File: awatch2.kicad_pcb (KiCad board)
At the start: 4 copper layers, 73.4 x 64.4 mm, 169 parts, among them J101 Conn_01x02, J102 Conn_01x02, J103 Conn_01x02, J104 Conn_01x02, J301 Conn_01x02, J801 Molex 1050170001, J802 Conn_01x06, Q701 FDV301N, SW101 B3S-1000, SW102 B3S-1000, SW103 B3S-1000, SW104 B3S-1000, U1 nRF52840, U301 MAX14690, U401 W25Q128JVPIQTR, U501 BMM150, U502 APDS-9306-065, U503 BMI160, U504 BMP388, U601 SPK0641HT4H-1, U701 AYF531035 (LS013B7DH05), U801 AT93C46DN-SH-T, U802 MCP1703A-3302_SOT223, U803 FT2232HL, U901 DRV2604, X1 ABM11W-32.0000MHZ-8-B1U-T3, Y801 FH1200004

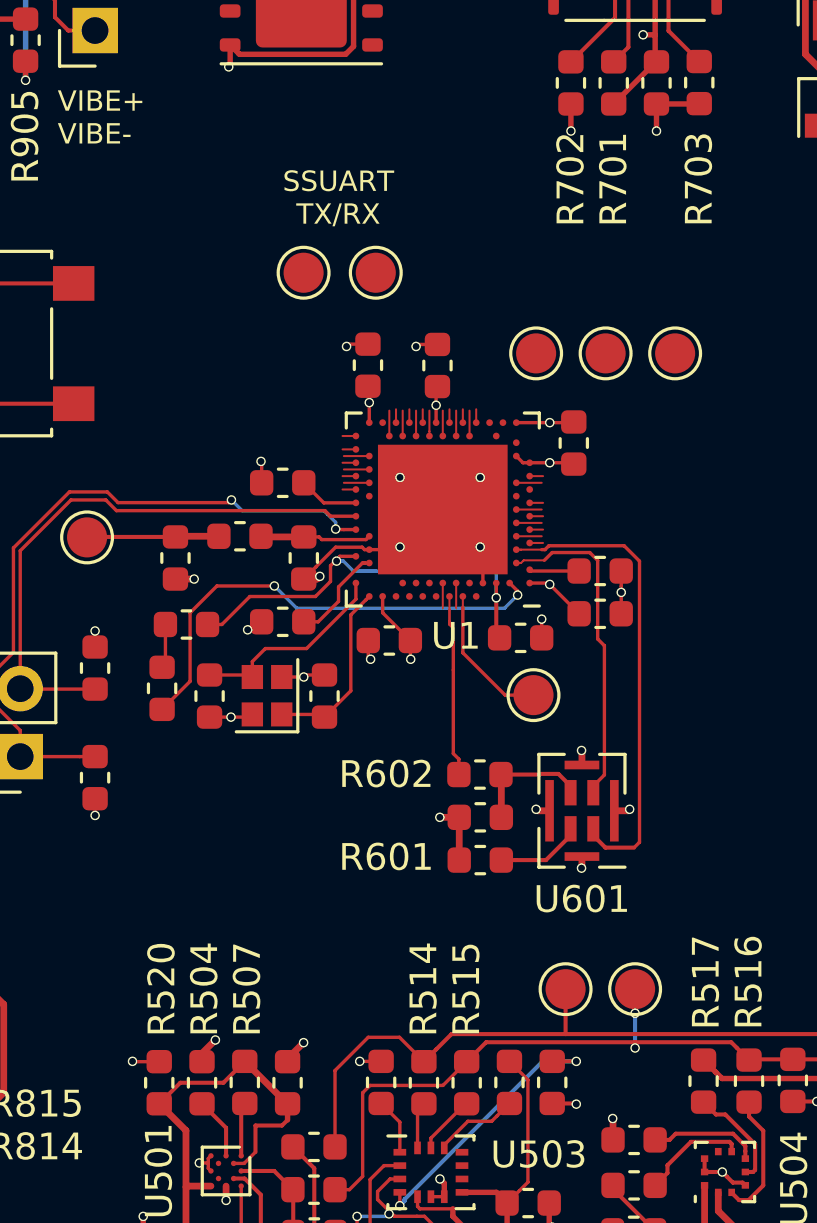
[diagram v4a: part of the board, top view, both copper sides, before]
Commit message: nRF pinout changes for routability
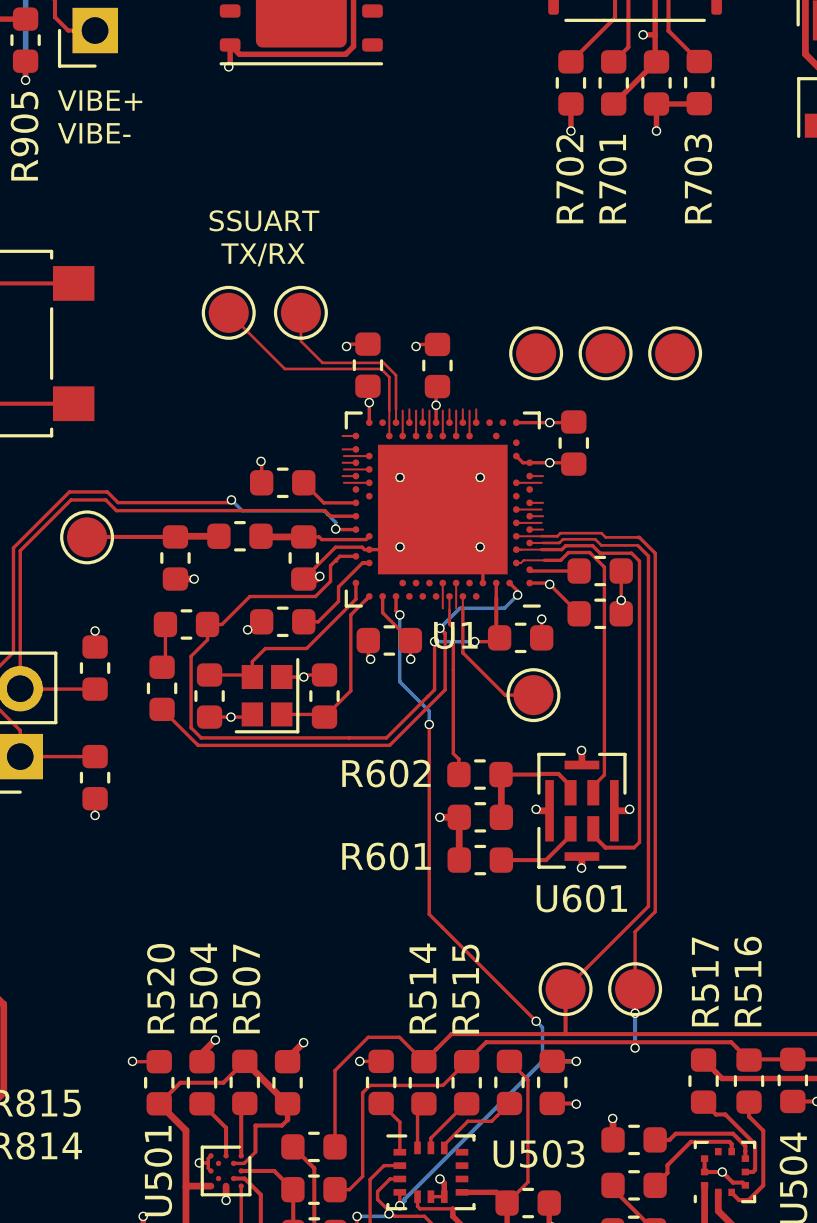
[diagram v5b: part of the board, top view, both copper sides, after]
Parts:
- moved TP108 3.18 mm to (81.5, 51.5)
- moved TP109 3.18 mm to (84.2, 51.5)
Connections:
- U1 pad A20: Net-(U1-PadA20) -> /Sensors/SENS_IMU_INT
- U1 pad G1: /FTDI USB Debug/UARTDBG_RX -> /Sensors/SENS_SDA
- U1 pad H2: /FTDI USB Debug/UARTDBG_TX -> /Sensors/SENS_SCL
- U1 pad L1: /Sensors/SENS_SCL -> /FTDI USB Debug/UARTDBG_RX
- U1 pad N1: /Sensors/SENS_SDA -> /FTDI USB Debug/UARTDBG_TX
- U1 pad R24: /Sensors/SENS_IMU_INT -> Net-(U1-PadR24)
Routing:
- net /Sensors/SENS_SDA: track 39.7 -> 61.5 mm
- net /Sensors/SENS_SCL: track 26.8 -> 48.5 mm
- net /Sensors/SENS_IMU_INT: track 10.8 -> 29.9 mm, vias 2 -> 5
- net Net-(C15-Pad2): track 16.2 -> 27.5 mm
- net /nRF52840/UARTSS_TX: track 0.95 -> 9.20 mm
- net /nRF52840/UARTSS_RX: track 0.50 -> 6.92 mm
- net Net-(L2-Pad2): track 17.8 -> 18.4 mm

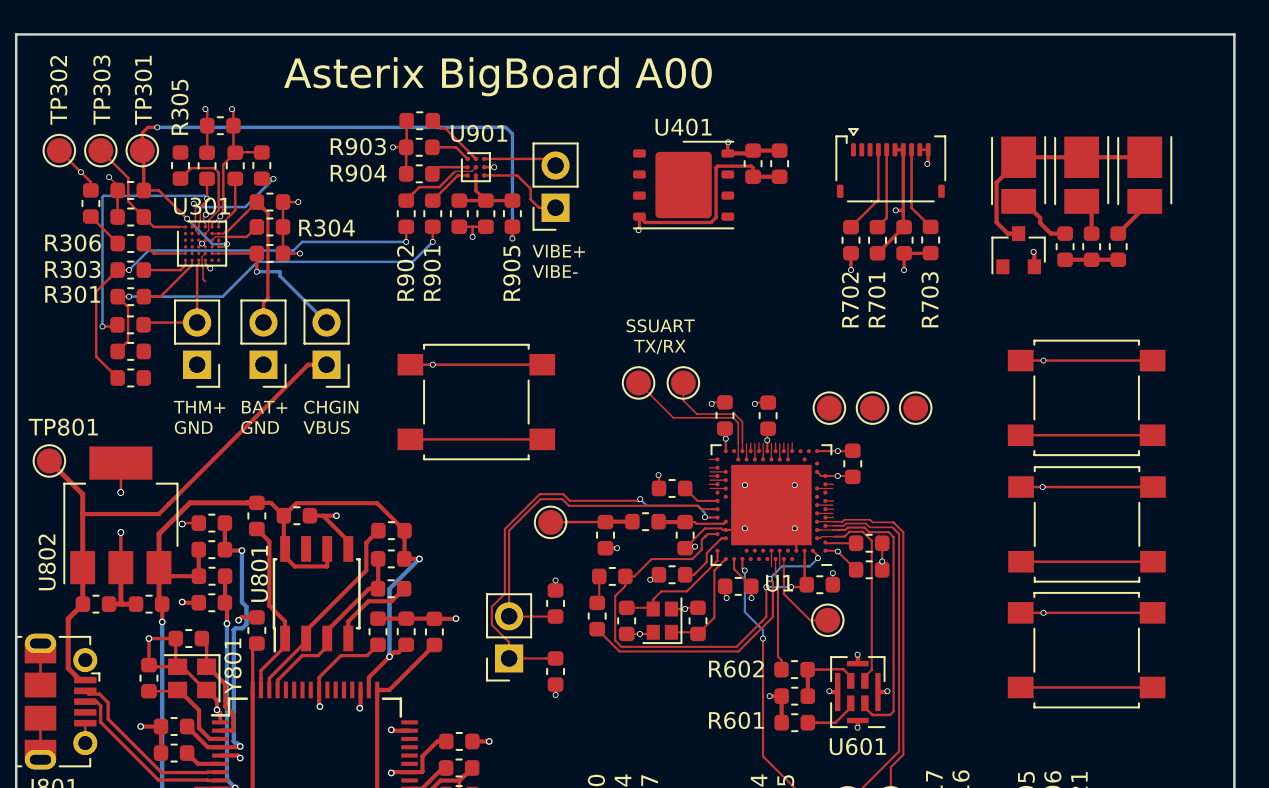
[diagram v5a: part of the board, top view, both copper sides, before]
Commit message: some PMIC and sensor routing
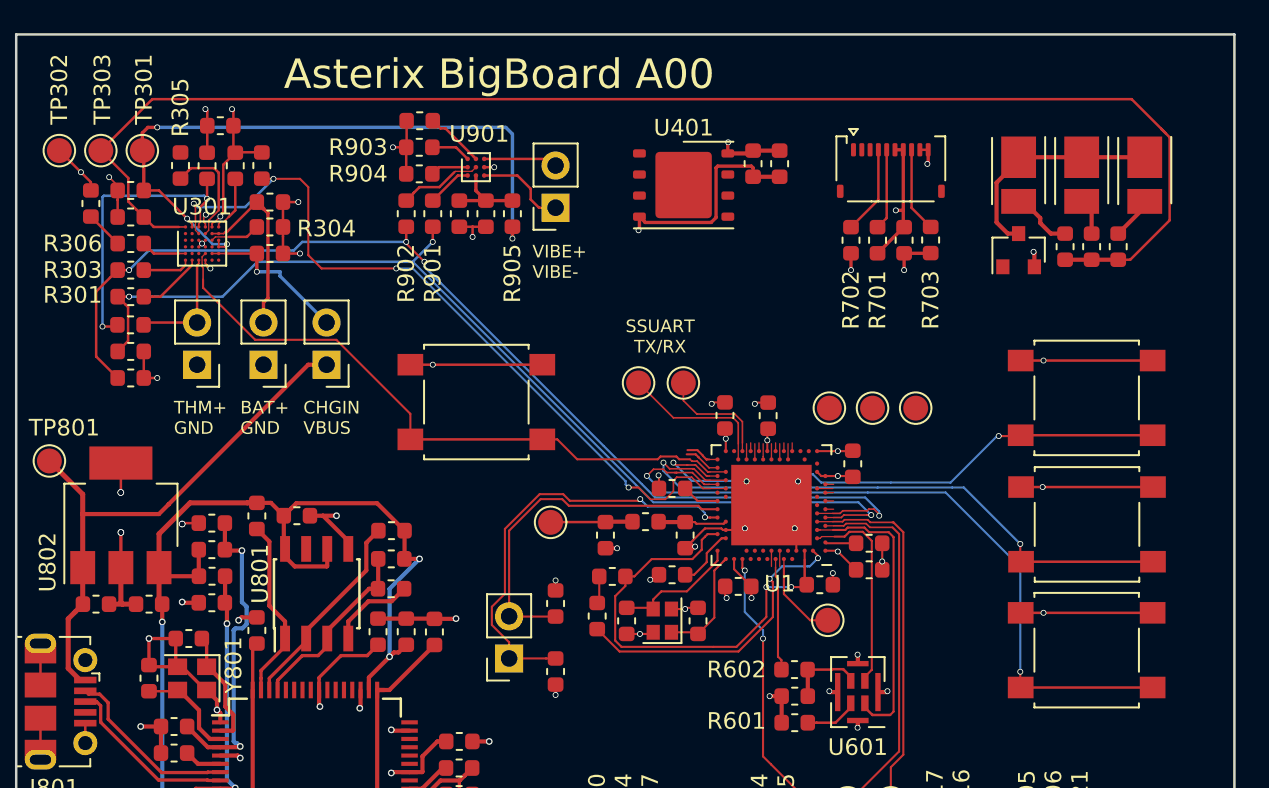
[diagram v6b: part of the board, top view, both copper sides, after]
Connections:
- U1 pad M2: /nRF52840/NRF_CHICKEN0 -> Net-(U1-PadM2)
- U1 pad R1: Net-(U1-PadR1) -> /nRF52840/NRF_CHICKEN0
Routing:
- net +3.3V: track 11.0 -> 87.1 mm
- net /PMIC/PMIC_SDA: track 27.5 -> 67.1 mm, vias 2 -> 4
- net /PMIC/PMIC_INTn: track 9.33 -> 47.4 mm, vias 2 -> 4
- net /nRF52840/BTN_DOWN: track 8.45 -> 44.9 mm, vias 0 -> 2
- net /PMIC/PMIC_SCL: track 25.6 -> 61.9 mm, vias 2 -> 3
- net /PMIC/BTN_BACK: track 10.8 -> 39.3 mm
- net /nRF52840/BTN_CENTER: track 8.90 -> 37.1 mm, vias 0 -> 2
- net /nRF52840/BTN_UP: track 8.45 -> 33.9 mm, vias 0 -> 2
- net +2V8: track 61.6 -> 64.0 mm, vias 22 -> 23
- net /FTDI USB Debug/NRF_SWDCLK: track 28.3 -> 30.0 mm
- net /FTDI USB Debug/NRF_SWDIO: track 35.0 -> 36.6 mm

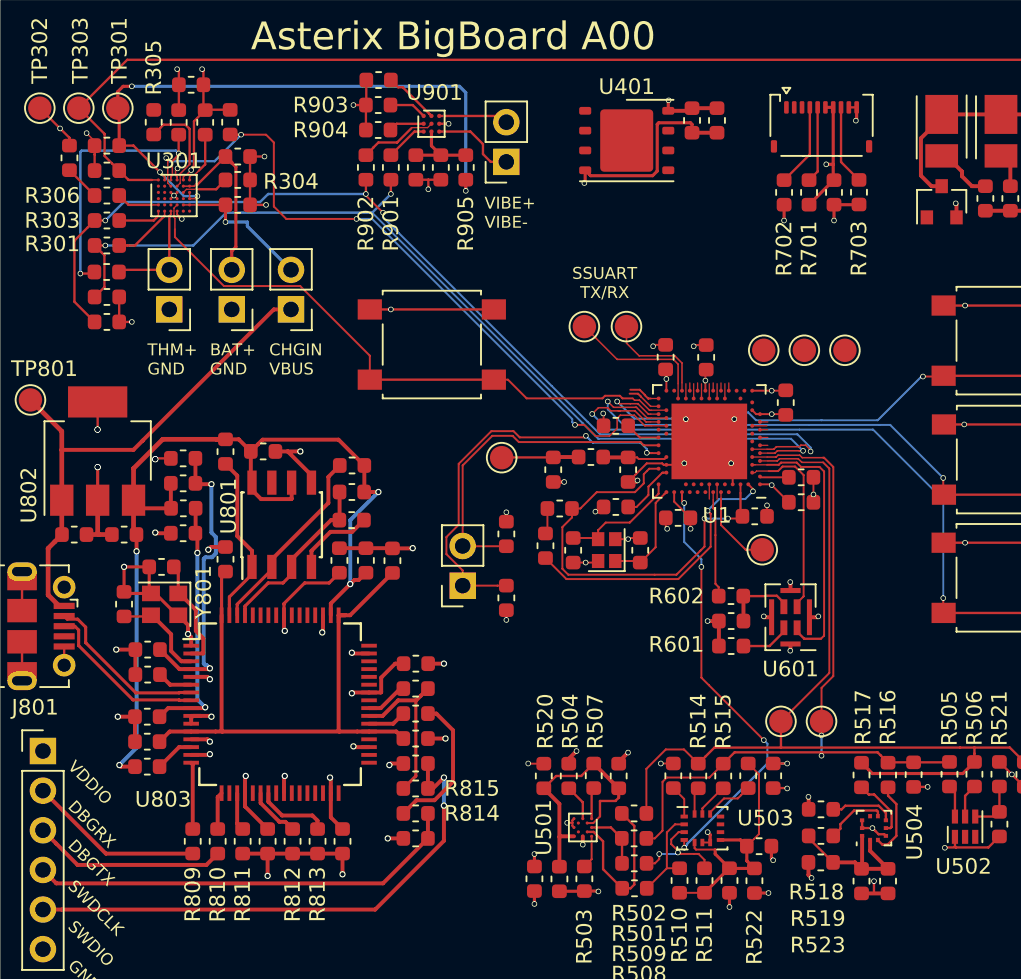
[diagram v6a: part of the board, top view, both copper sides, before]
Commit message: fully routed
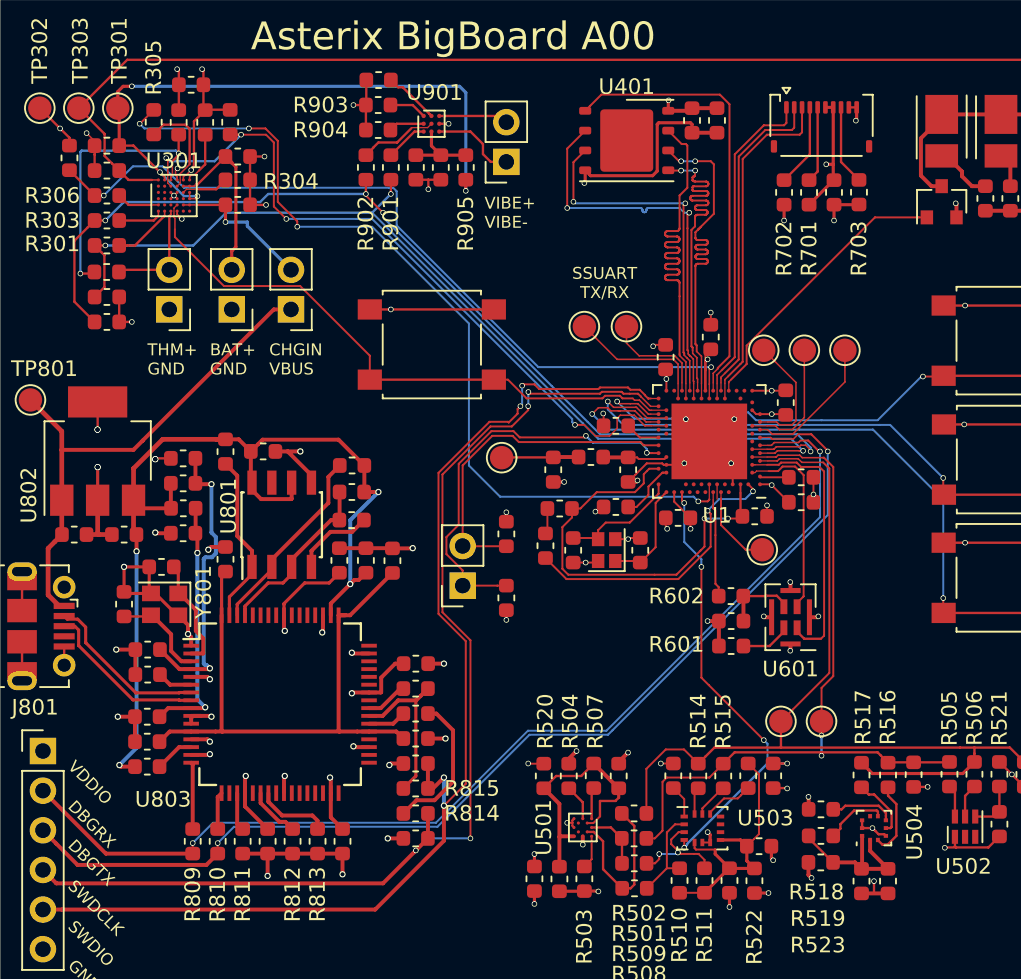
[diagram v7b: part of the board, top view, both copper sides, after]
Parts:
- moved C7 1.33 mm to (89.6, 52.2)
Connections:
- U1 pad AC11: /Display/DISP_MOSI -> /Display/DISP_SCK
- U1 pad AD10: /Display/DISP_SCK -> /Display/DISP_MOSI
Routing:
- net /FTDI USB Debug/UARTDBG_RX: track 11.8 -> 69.3 mm, vias 0 -> 2
- net /FTDI USB Debug/UARTDBG_TX: track 12.9 -> 70.0 mm, vias 0 -> 2
- net /PMIC/PMIC_SENS: track 0.95 -> 56.7 mm, vias 0 -> 4
- net /PMIC/NRF_RESETN: track 3.24 -> 51.3 mm, vias 0 -> 2
- net /FTDI USB Debug/NRF_SWDCLK: track 30.0 -> 72.9 mm, vias 0 -> 4
- net /FTDI USB Debug/NRF_SWDIO: track 36.6 -> 75.0 mm, vias 2 -> 4
- net /SPI Flash/FLASH_CSN: track 0.50 -> 28.7 mm
- net /SPI Flash/FLASH_D3: track 0.95 -> 26.1 mm
- net /SPI Flash/FLASH_D1: track 0.95 -> 26.0 mm, vias 0 -> 2
- net /SPI Flash/FLASH_D0: track 0.50 -> 23.1 mm, vias 0 -> 2
- net /SPI Flash/FLASH_D2: track 0.50 -> 23.0 mm, vias 0 -> 2
- net /SPI Flash/FLASH_SCK: track 0.95 -> 23.2 mm, vias 0 -> 2
- net /Display/DISP_CSN: track 0.95 -> 21.9 mm
- net /Display/DISP_SCK: track 0.50 -> 21.3 mm
- net /Display/DISP_MOSI: track 0.95 -> 21.1 mm
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
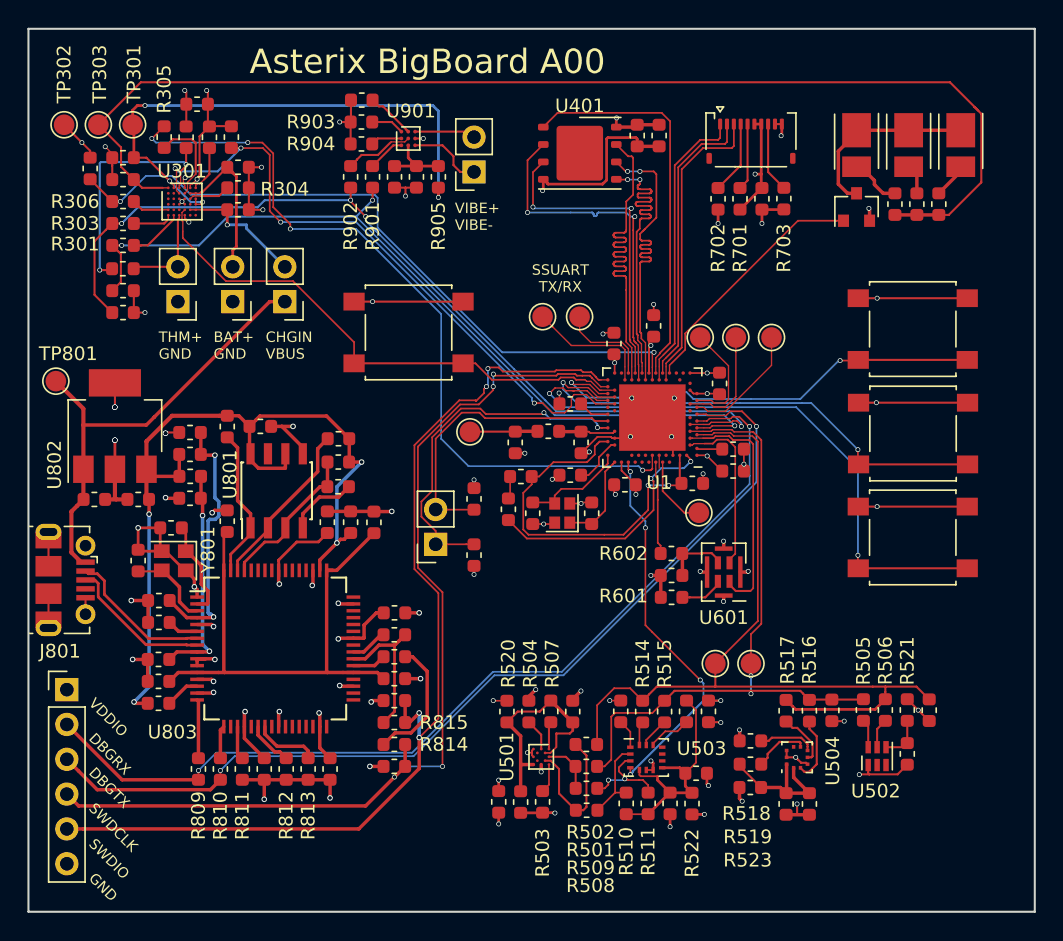
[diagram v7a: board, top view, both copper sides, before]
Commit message: passes DRC; top and bottom ground planes added
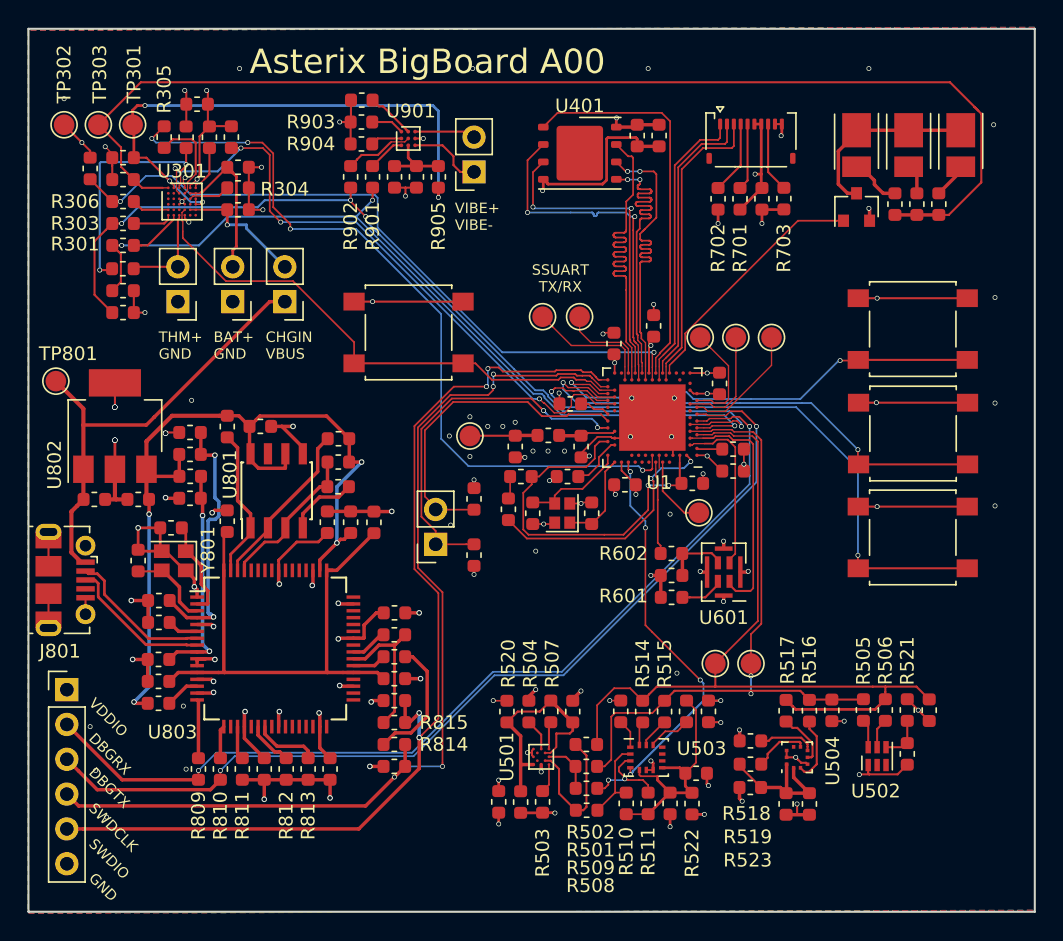
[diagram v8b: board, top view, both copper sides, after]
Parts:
- moved TP105 0.30 mm to (76.2, 60.2)
- moved C3 0.30 mm to (84.3, 61.0)
- moved C4 0.30 mm to (79.5, 61.0)
- moved L1 0.30 mm to (81.9, 60.2)
- moved C11 0.22 mm to (83.3, 63.2)
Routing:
- net /nRF52840/NRF_NFC1: track 21.6 -> 23.8 mm
- net /nRF52840/NRF_NFC2: track 25.9 -> 27.2 mm
- net /FTDI USB Debug/NRF_SWDCLK: track 72.9 -> 73.7 mm
- net /FTDI USB Debug/NRF_SWDIO: track 75.0 -> 75.6 mm
- net GND: vias 86 -> 114
- added copper zone on B.Cu, net GND
- added copper zone on F.Cu, net GND
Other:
- net class MAX14690: clearance 0.127 -> 0.0635
- net class Magnetometer 4/4: clearance 0.127 -> 0.1016
- net class NRF 3/3: clearance 0.127 -> 0.0762
- net class Vibe 2.75: clearance 0.127 -> 0.06985
